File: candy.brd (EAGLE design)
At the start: 26 x 26 mm, 8 parts

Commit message: board ready for silk
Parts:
- 2N2222: device transistor-neu-to92:TO92-EBC -> TinyTony_ShenzenReady:TO92-EBC
- moved U$4 41.0 mm to (12.8, 18.8)
- moved U$7 40.6 mm to (12.7, 12.6)
- moved U$5 40.5 mm to (20.3, 19.8)
- moved VCC 39.2 mm to (5.53, 19.7)
- moved N-MOSFET 38.1 mm to (12.8, 14.1)
- moved 10M 37.3 mm to (12.8, 9.83)
- moved U$1 35.3 mm to (7.47, 13.2)
- moved 2N2222 34.1 mm to (12.8, 3.02), turned to 180 degrees
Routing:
- net LOAD: track 7.50 -> 17.9 mm
- net GND: track 0.00 -> 5.52 mm, vias 0 -> 1
- net VCC: track 20.5 -> 16.6 mm, vias 4 -> 2
- net N$1: track 13.1 -> 13.8 mm
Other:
- board size 26 x 26 mm -> 28 x 28 mm
- board text added: "G:/_GIT/candy/artwork.bmp"

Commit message: shifted a bit
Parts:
- moved U$1 2.17 mm to (6.71, 11.1)
- moved N-MOSFET 1.33 mm to (12.5, 12.8)
- moved VCC 0.94 mm to (5.62, 18.8)
- moved 10M 0.81 mm to (12.8, 9.02)
- moved U$4 0.68 mm to (12.8, 18.1)
- moved 2N2222 0.48 mm to (12.4, 2.68)
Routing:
- net GND: track 5.52 -> 10.9 mm
- net LOAD: track 17.9 -> 21.5 mm
- net VCC: track 16.6 -> 17.6 mm
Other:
- board text added: "G:/_GIT/candy/gfx/artwork-draw.bmp"

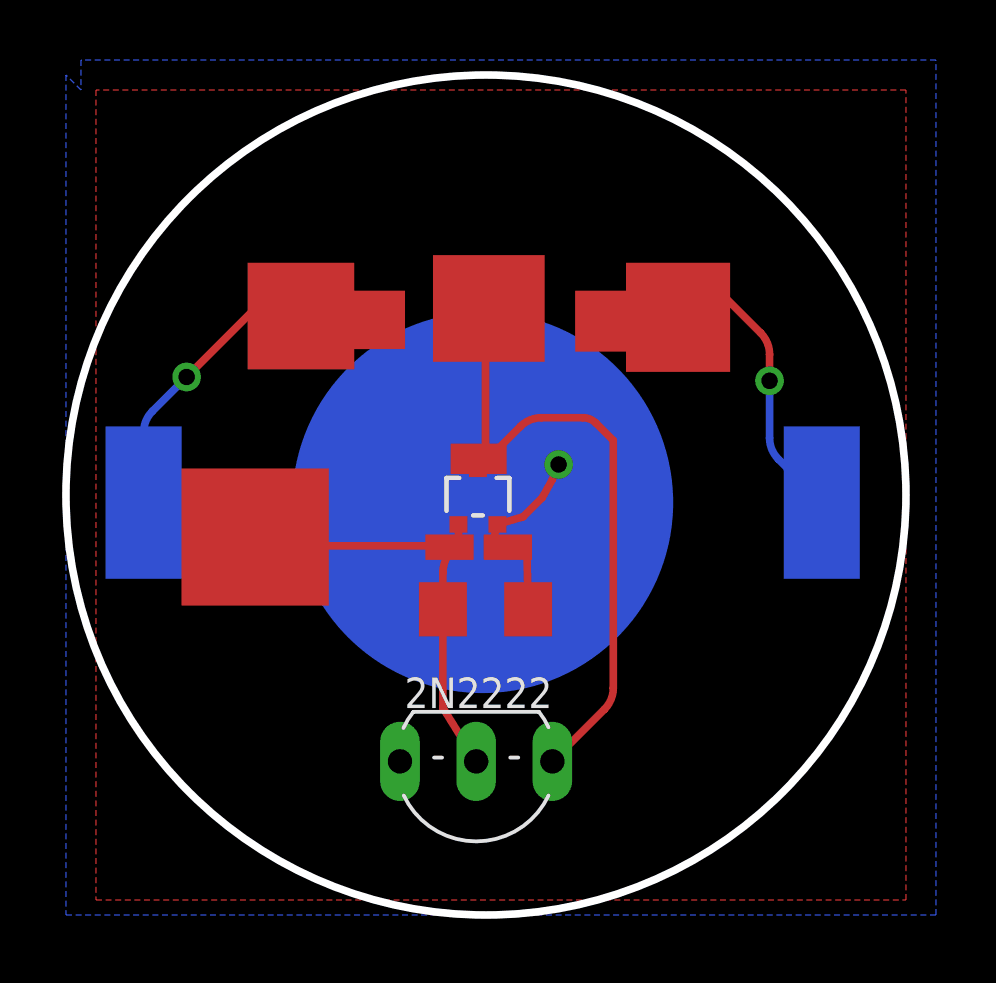
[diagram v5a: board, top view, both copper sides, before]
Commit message: no pours, smd and npn
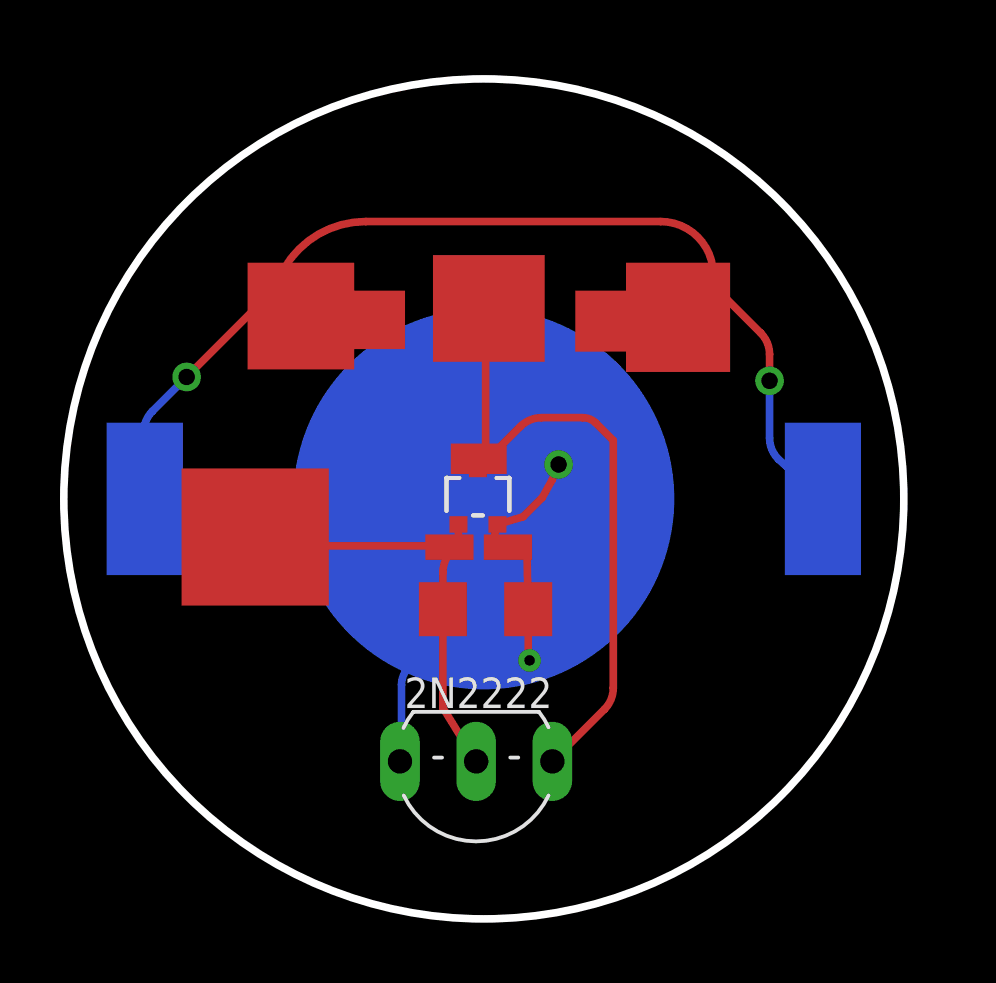
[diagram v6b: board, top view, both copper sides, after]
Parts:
- moved U$7 0.13 mm to (12.7, 12.7)
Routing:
- net VCC: track 17.6 -> 34.5 mm
- net GND: track 10.9 -> 19.7 mm, vias 1 -> 2
- removed copper zone on layer 16, net GND
- removed copper zone on layer 1, net VCC
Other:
- board text removed: "G:/_GIT/candy/gfx/artwork-draw.bmp"

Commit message: stick on front
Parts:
- removed 2N2222: (no value), TinyTony_ShenzenReady:TO92-EBC
- moved U$4 0.32 mm to (12.7, 17.8)
- moved N-MOSFET 0.21 mm to (12.7, 12.7)
- moved 10M 0.06 mm to (12.7, 9.02)
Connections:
- net GND: now also U$7.-; no longer 2N2222.C, U$7.P$1-
- net LOAD: no longer 2N2222.E
- net N$1: no longer 2N2222.B
- net VCC: now also U$7.+, U$7.+2; no longer U$7.P$2+, U$7.P$3+
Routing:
- net LOAD: track 21.5 -> 4.44 mm
- net GND: track 19.7 -> 4.66 mm, vias 2 -> 1
- net N$1: track 13.3 -> 7.84 mm
- net VCC: track 34.5 -> 36.3 mm

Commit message: gerber ready
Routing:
- net VCC: track 36.3 -> 70.2 mm
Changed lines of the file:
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@@
 <setting verticaltext="up"/>
 </settings>
-<grid distance="5" unitdist="mil" unit="mm" style="lines" multiple="1" display="yes" altdistance="1" altunitdist="mil" altunit="mil"/>
+<grid distance="5" unitdist="mil" unit="mil" style="lines" multiple="1" display="yes" altdistance="1" altunitdist="mil" altunit="mil"/>
 <layers>
 <layer number="1" name="Top" color="4" fill="1" visible="yes" active="yes"/>
@@
 <layer number="27" name="tValues" color="7" fill="1" visible="no" active="yes"/>
 <layer number="28" name="bValues" color="7" fill="1" visible="no" active="yes"/>
-<layer number="29" name="tStop" color="7" fill="3" visible="no" active="yes"/>
+<layer number="29" name="tStop" color="7" fill="3" visible="yes" active="yes"/>
 <layer number="30" name="bStop" color="7" fill="6" visible="no" active="yes"/>
 <layer number="31" name="tCream" color="7" fill="4" visible="no" active="yes"/>
@@
 <board>
 <plain>
-<circle x="12.7" y="12.7" radius="14" width="0.254" layer="20"/>
+<circle x="12.7" y="12.7" radius="14" width="0.1" layer="20"/>
 <rectangle x1="11.811" y1="-0.04241875" x2="13.843" y2="0.04241875" layer="200"/>
 <rectangle x1="11.049" y1="0.04241875" x2="14.605" y2="0.127" layer="200"/>
@@
 <rectangle x1="11.43" y1="13.716" x2="13.97" y2="14.732" layer="29"/>
 <rectangle x1="11.43" y1="13.716" x2="13.97" y2="14.732" layer="1"/>
-<rectangle x1="11.684" y1="-0.762" x2="14.224" y2="5.334" layer="1"/>
-<hole x="14.859" y="1.397" drill="0.65"/>
-<hole x="11.176" y="1.397" drill="0.65"/>
+<rectangle x1="11.684" y1="-0.762" x2="13.716" y2="5.334" layer="1"/>
+<hole x="14.351" y="0.254" drill="0.65"/>
+<hole x="11.049" y="0.254" drill="0.65"/>
+<rectangle x1="11.684" y1="-0.889" x2="13.716" y2="5.334" layer="29"/>
 </plain>
 <attributes>
@@
 <contactref element="U$7" pad="+"/>
 <wire x1="5.61706875" y1="18.7985125" x2="5.61706875" y2="19.33306875" width="0.2032" layer="1"/>
-<wire x1="5.61706875" y1="19.33306875" x2="8.636" y2="22.352" width="0.3048" layer="1" curve="-90"/>
-<wire x1="8.636" y1="22.352" x2="17.808375" y2="22.352" width="0.3048" layer="1"/>
-<wire x1="17.808375" y1="22.352" x2="20.345959375" y2="19.814415625" width="0.3048" layer="1" curve="-90"/>
-<wire x1="3.81" y1="18.796" x2="5.61455625" y2="18.796" width="0.3048" layer="1"/>
+<wire x1="5.61706875" y1="19.33306875" x2="8.636" y2="22.352" width="0.6096" layer="1" curve="-90"/>
+<wire x1="8.636" y1="22.352" x2="17.808375" y2="22.352" width="0.6096" layer="1"/>
+<wire x1="17.808375" y1="22.352" x2="20.345959375" y2="19.814415625" width="0.6096" layer="1" curve="-90"/>
+<wire x1="3.81" y1="18.796" x2="5.61455625" y2="18.796" width="0.6096" layer="1"/>
 <wire x1="5.61455625" y1="18.796" x2="5.61706875" y2="18.7985125" width="0.2032" layer="1" curve="90"/>
-<wire x1="22.098" y1="18.542" x2="20.828" y2="18.542" width="0.3048" layer="1"/>
+<wire x1="22.098" y1="18.542" x2="20.828" y2="18.542" width="0.6096" layer="1"/>
 <wire x1="20.828" y1="18.542" x2="20.32" y2="19.05" width="0.2032" layer="1" curve="-90"/>
 <wire x1="20.32" y1="19.05" x2="20.32" y2="19.78845625" width="0.2032" layer="1"/>
@@
 <wire x1="0.889" y1="12.7" x2="0.889" y2="13.462" width="0.2032" layer="16"/>
 <via x="0.889" y="13.462" extent="1-16" drill="0.35"/>
-<wire x1="0.889" y1="13.462" x2="0.889" y2="15.875" width="0.3048" layer="1"/>
-<wire x1="0.889" y1="15.875" x2="3.81" y2="18.796" width="0.3048" layer="1" curve="-90"/>
+<wire x1="0.889" y1="13.462" x2="0.889" y2="15.875" width="0.6096" layer="1"/>
+<wire x1="0.889" y1="15.875" x2="3.81" y2="18.796" width="0.6096" layer="1" curve="-90"/>
 <via x="24.511" y="12.7" extent="1-16" drill="0.35"/>
-<wire x1="24.511" y1="12.7" x2="24.511" y2="16.129" width="0.3048" layer="1"/>
-<wire x1="24.511" y1="16.129" x2="22.098" y2="18.542" width="0.3048" layer="1" curve="90"/>
+<wire x1="24.511" y1="12.7" x2="24.511" y2="16.129" width="0.6096" layer="1"/>
+<wire x1="24.511" y1="16.129" x2="22.098" y2="18.542" width="0.6096" layer="1" curve="90"/>
+<wire x1="24.511" y1="12.7" x2="13.716" y2="1.651" width="0.6096" layer="1" curve="-90"/>
+<wire x1="11.684" y1="1.651" x2="0.762" y2="12.573" width="0.6096" layer="1" curve="-90"/>
+<wire x1="0.762" y1="12.573" x2="0.762" y2="13.335" width="0.6096" layer="1"/>
+<wire x1="0.762" y1="13.335" x2="0.889" y2="13.462" width="0.1524" layer="1" curve="-90"/>
+<wire x1="13.716" y1="1.651" x2="11.684" y2="1.651" width="0.1524" layer="1"/>
 </signal>
 </signals>
